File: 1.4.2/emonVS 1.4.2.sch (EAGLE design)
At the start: 46 parts, among them J7 RJ45 Jack, J8 TERMINAL_BLOCK_2P, J9 TERMINAL_BLOCK_5P, M1 275VAC, M2 275VAC, M3 275VAC, T1 ZMPT101B, T2 ZMPT101B, T3 ZMPT101B

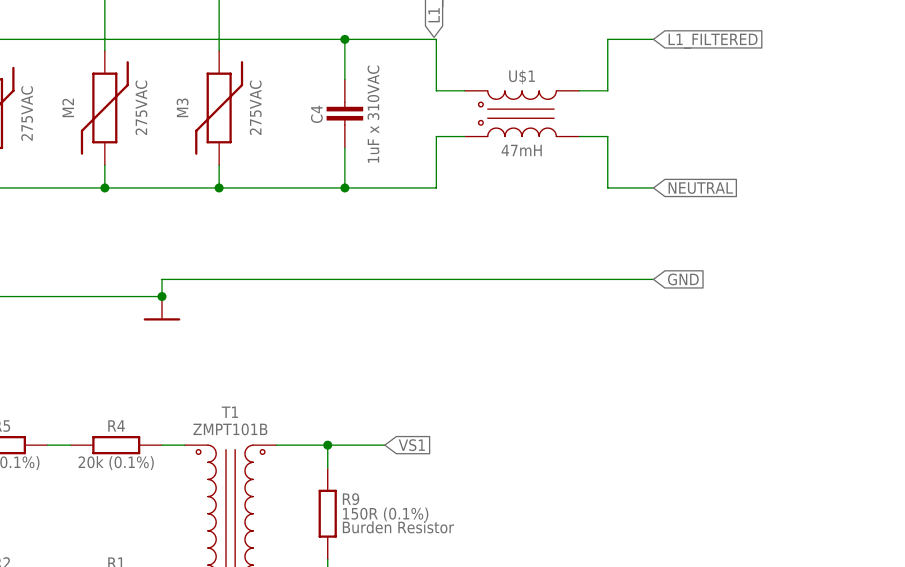
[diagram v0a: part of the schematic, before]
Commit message: connect GND via solder jumper
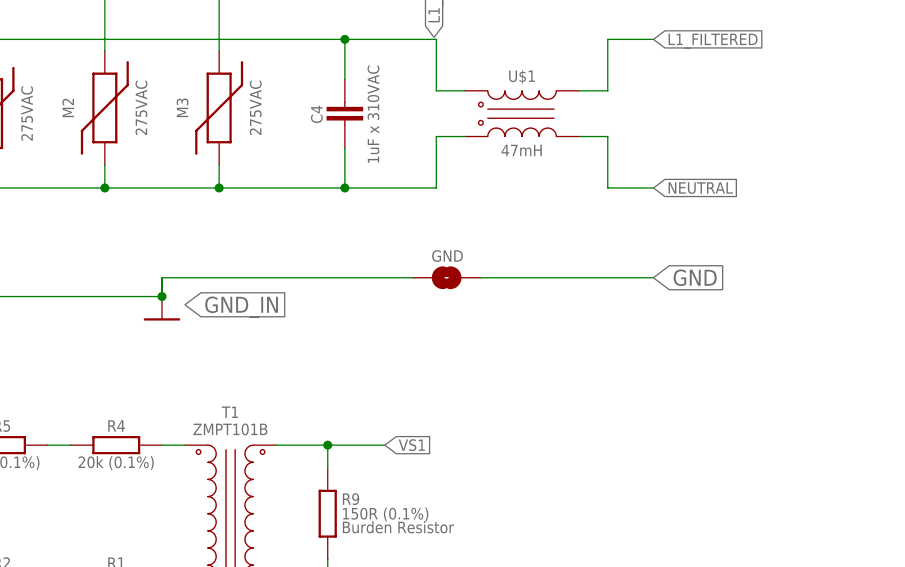
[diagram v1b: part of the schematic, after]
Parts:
- added GND: SOLDER_JUMPER_2P_NO, OpenEnergyMonitor:SOLDER_JUMPER_2P_NO
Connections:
- new net GND_IN: GND.1, J9-2.P$1
- net GND: now also GND.2; no longer J9-2.P$1
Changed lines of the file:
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@@
 <part name="SUPPLY7" library="My-Supply" library_urn="urn:adsk.eagle:library:35531236" deviceset="0V" device=""/>
 <part name="SUPPLY8" library="My-Supply" library_urn="urn:adsk.eagle:library:35531236" deviceset="5V" device=""/>
+<part name="GND" library="OpenEnergyMonitor" deviceset="SOLDER_JUMPER_2P_NO" device="" value="SOLDER_JUMPER_2P_NO"/>
 </parts>
 <sheets>
@@
 <instance part="SUPPLY8" gate="G$1" x="178.435" y="115.57" smashed="yes" rot="MR0" grouprefs="OUTPUT_SIGNALS_AND_SUPPLY">
 <attribute name="VALUE" x="178.4096" y="119.38" size="1.27" layer="96" rot="MR0" align="center"/>
+</instance>
+<instance part="GND" gate="G$1" x="91.317609375" y="115.11870625" smashed="yes">
+<attribute name="NAME" x="91.41184375" y="117.534603125" size="1.27" layer="95" align="center"/>
 </instance>
 </instances>
@@
 </segment>
 <segment>
-<label x="114.3" y="114.935" size="1.27" layer="95" xref="yes" grouprefs="THREE-PHASE_AC_NETWORK_INTERFACE"/>
-<pinref part="SUPPLY6" gate="G$1" pin="0V"/>
-<wire x1="59.69" y1="114.935" x2="114.3" y2="114.935" width="0.1524" layer="91" grouprefs="THREE-PHASE_AC_NETWORK_INTERFACE"/>
-<wire x1="59.69" y1="113.03" x2="59.69" y2="114.935" width="0.1524" layer="91" grouprefs="THREE-PHASE_AC_NETWORK_INTERFACE"/>
-<wire x1="59.69" y1="113.03" x2="29.5" y2="113.03" width="0.1524" layer="91"/>
-<wire x1="29.5" y1="113.03" x2="29.5" y2="125.1" width="0.1524" layer="91"/>
-<junction x="59.69" y="113.03"/>
-<pinref part="J9" gate="-2" pin="P$1"/>
-<wire x1="29.5" y1="125.1" x2="18.415" y2="125.1" width="0.1524" layer="91"/>
-<wire x1="18.415" y1="125.1" x2="18.415" y2="125.095" width="0.1524" layer="91"/>
-</segment>
-<segment>
 <pinref part="SJ3" gate="1" pin="1"/>
 <pinref part="L1" gate="G$1" pin="4"/>
@@
 <wire x1="178.435" y1="73.025" x2="178.435" y2="86.36" width="0.1524" layer="91" grouprefs="OUTPUT_SIGNALS_AND_SUPPLY"/>
 <junction x="178.435" y="86.36" grouprefs="OUTPUT_SIGNALS_AND_SUPPLY"/>
+</segment>
+<segment>
+<pinref part="GND" gate="G$1" pin="2"/>
+<wire x1="95.127609375" y1="115.11870625" x2="114.22185" y2="115.11870625" width="0.1524" layer="91"/>
+<label x="114.283696875" y="115.1201875" size="1.778" layer="95" xref="yes"/>
 </segment>
 </net>
@@
 </segment>
 </net>
+<net name="GND_IN" class="0">
+<segment>
+<pinref part="SUPPLY6" gate="G$1" pin="0V"/>
+<wire x1="59.69" y1="113.03" x2="59.69" y2="114.935" width="0.1524" layer="91" grouprefs="THREE-PHASE_AC_NETWORK_INTERFACE"/>
+<wire x1="59.69" y1="113.03" x2="29.5" y2="113.03" width="0.1524" layer="91"/>
+<wire x1="29.5" y1="113.03" x2="29.5" y2="125.1" width="0.1524" layer="91"/>
+<junction x="59.69" y="113.03"/>
+<pinref part="J9" gate="-2" pin="P$1"/>
+<wire x1="29.5" y1="125.1" x2="18.415" y2="125.1" width="0.1524" layer="91"/>
+<wire x1="18.415" y1="125.1" x2="18.415" y2="125.095" width="0.1524" layer="91"/>
+<pinref part="GND" gate="G$1" pin="1"/>
+<wire x1="87.507609375" y1="115.11870625" x2="59.69" y2="115.11870625" width="0.1524" layer="91"/>
+<wire x1="59.69" y1="115.11870625" x2="59.69" y2="113.03" width="0.1524" layer="91"/>
+<label x="62.235346875" y="112.115753125" size="1.778" layer="95" xref="yes"/>
+</segment>
+</net>
